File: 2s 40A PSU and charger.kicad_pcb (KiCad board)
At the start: 4 copper layers, 45 x 20 mm, 112 parts, among them J1 Keystone 3579, J10 G-Switch-GT-USB-7025, J11 1.27mm 4 pin socket, J12 USB, J2 JST XH-S Balance Plug, J3 Keystone 3579, J4 Keystone 3569, J5 Keystone 3569, J6 Keystone 3579, J7 Keystone 3579, J8 Keystone 3569, J9 Keystone 3569, Q1 PJA3430, or HL 2320A, Q2 PJA3430, or HL 2320A, Q3 Vishay sir404dp, or SiR500DP, Q4 PJA3430, or HL 2320A, Q5 PJA3430, or HL 2320A, Q6 Vishay sir404dp, or SiR500DP, U1 BQ76905RGRR, U2 AP63203WU, U3 BQ24780SRUYR, U5 THVD1420DRLR, U6 CH32X035G8U6, U7 TPS7A2633DRV

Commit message: Started layout of new components
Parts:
- added R13: 10k, Resistor_SMD:R_0402_1005Metric, B.Cu at (116.9, 130.9)
- added R32: 10k, Resistor_SMD:R_0402_1005Metric, B.Cu at (111.6, 128.1)
- added SW1: Mitsumi R-667996, Misumi switches:R-667995_MIT, B.Cu at (119.6, 130.8)
- J1, J3, J6, J7: value Keystone 3579 -> Keystone 6100; footprint custom_Connector:Keystone_3579 -> custom_Connector:Keystone_6100
- J4, J5, J8, J9: value Keystone 3569 -> Keystone 6102; footprint custom_Connector:Keystone_3569_half -> custom_Connector:Keystone_6102
- L3: value 2.2uH, WIP322512A-2R2MLDG -> 2.7uH
- U6: footprint Package_DFN_QFN:QFN-28-1EP_4x4mm_P0.4mm_EP2.8x2.8mm -> qfn_custom:QFN-28-1EP_4x4mm_P0.4mm_EP2.8x2.8mm
- moved R31 0.45 mm to (115.1, 130.9)
- moved R30 0.43 mm to (113.3, 131.0)
- moved D2 0.39 mm to (111.2, 129.8)
- moved U2 0.18 mm to (134.1, 121.0)
- moved C40 0.17 mm to (133.5, 118.5)
- moved L3 0.15 mm to (130.7, 120.8)
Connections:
- net /Battery Balancer/+BAT renamed +BATT
- net /Battery Balancer/-BAT renamed -BATT
- net /Battery Balancer/Balancer Alert renamed /Balancer_Alert
- net /Battery Balancer/Bat Cell 1 renamed /Bat Cell 1
- net /Battery Charger/Always On PWR renamed Always On PWR
- net /Battery Charger/Charger IADP renamed /Charger_IADP
- net /Battery Charger/Charger IDCHG renamed /Charger_IDCHG
- net /Battery Charger/Charger PROCHOT renamed /Charger_PROCHOT
- net /Battery Charger/IN renamed USBPWR
- net /Battery Charger/MCU3.3v renamed Always On 3v3
- net /Battery Charger/PWRON renamed /PWRON
- net /Connectors/3.3v renamed Main 3v3
- net /Connectors/CC1 renamed /CC1
- net /Connectors/CC2 renamed /CC2
- net /Connectors/D+ renamed /D+
- net /Connectors/D- renamed /D-
- net /Connectors/RS485+ renamed /RS485+
- net /Connectors/RS485- renamed /RS485-
- C12 pad 2: /Battery Charger/MOTORPWR -> MOTORPWR
- C14 pad 2: /Battery Charger/MOTORPWR -> MOTORPWR
- C28 pad 1: /Battery Charger/MOTORPWR -> MOTORPWR
- J1 pad 1: /Battery Charger/MOTORPWR -> MOTORPWR
- J3 pad 1: /Battery Charger/MOTORPWR -> MOTORPWR
- J4 pad 1: /Battery Charger/MOTORPWR -> MOTORPWR
- J5 pad 1: /Battery Charger/MOTORPWR -> MOTORPWR
- NT3 pad 2: /Battery Charger/MOTORPWR -> MOTORPWR
- NT4 pad 2: /Battery Charger/MOTORPWR -> MOTORPWR
- Q3 pad 5: /Battery Charger/MOTORPWR -> MOTORPWR
- R1 pad 1: /Battery Charger/MOTORPWR -> MOTORPWR
- U2 pad 2: /Battery Charger/MOTORPWR -> /3v3_Main_EN
- U2 pad 3: /Battery Charger/MOTORPWR -> MOTORPWR
- U6 pad 23: unconnected-(U6-PB12-Pad23) -> /3v3_Main_EN
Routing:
- net /Battery Charger/MOTORPWR: track 10.7 -> 0.00 mm, vias 1 -> 0
- net MOTORPWR: track 0.00 -> 9.46 mm, vias 0 -> 1
- net Always On 3v3: track 43.8 -> 52.3 mm
- net /3v3_Main_EN: track 0.00 -> 6.62 mm, vias 0 -> 1
- net GND: track 66.4 -> 70.2 mm, vias 47 -> 46
- net Main 3v3: track 32.4 -> 33.9 mm
- net +BATT: track 63.7 -> 62.4 mm
- net Net-(R13-Pad1): track 0.00 -> 1.26 mm
- net /D+: track 23.4 -> 24.1 mm, vias 1 -> 2
- net Net-(U3-CMPIN): track 4.11 -> 3.40 mm
- added copper zone on F.Cu, net MOTORPWR
- removed copper zone on F.Cu, net /Battery Charger/MOTORPWR

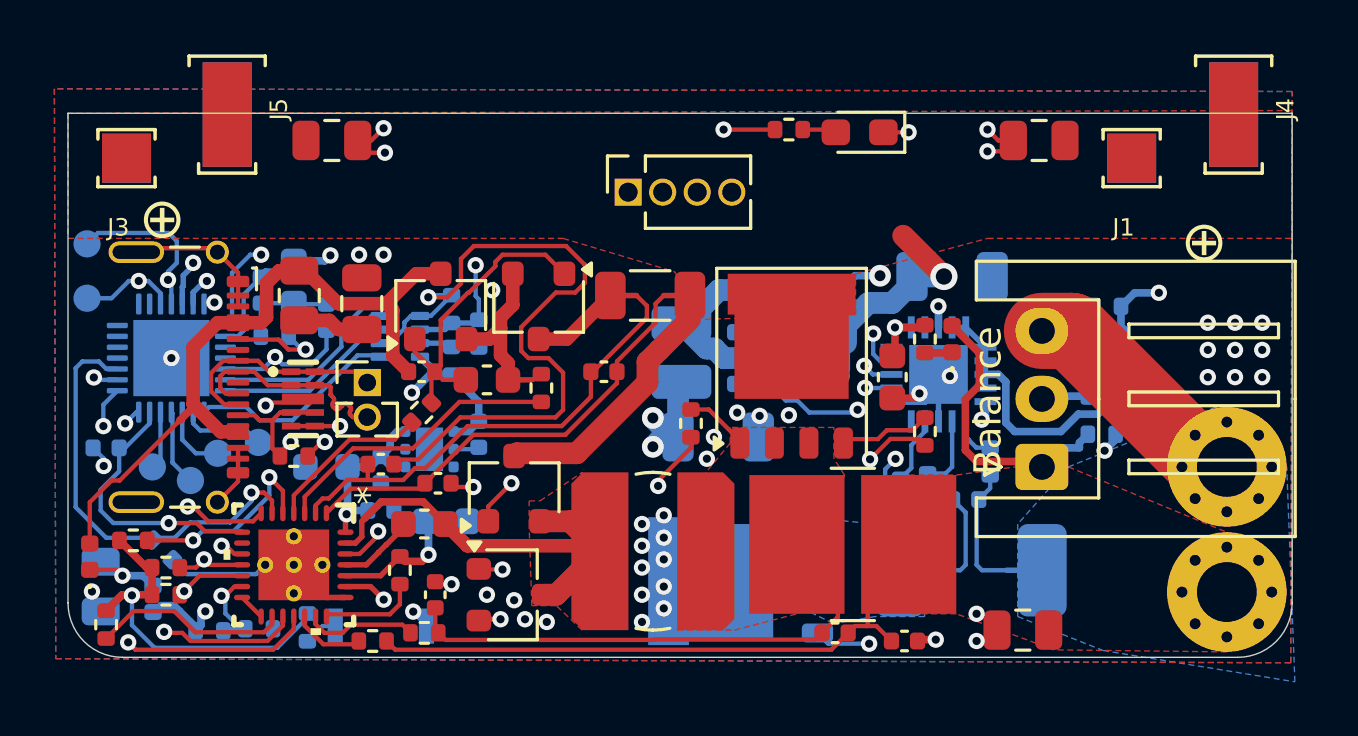
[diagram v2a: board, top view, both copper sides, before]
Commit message: Finished reroute and placement
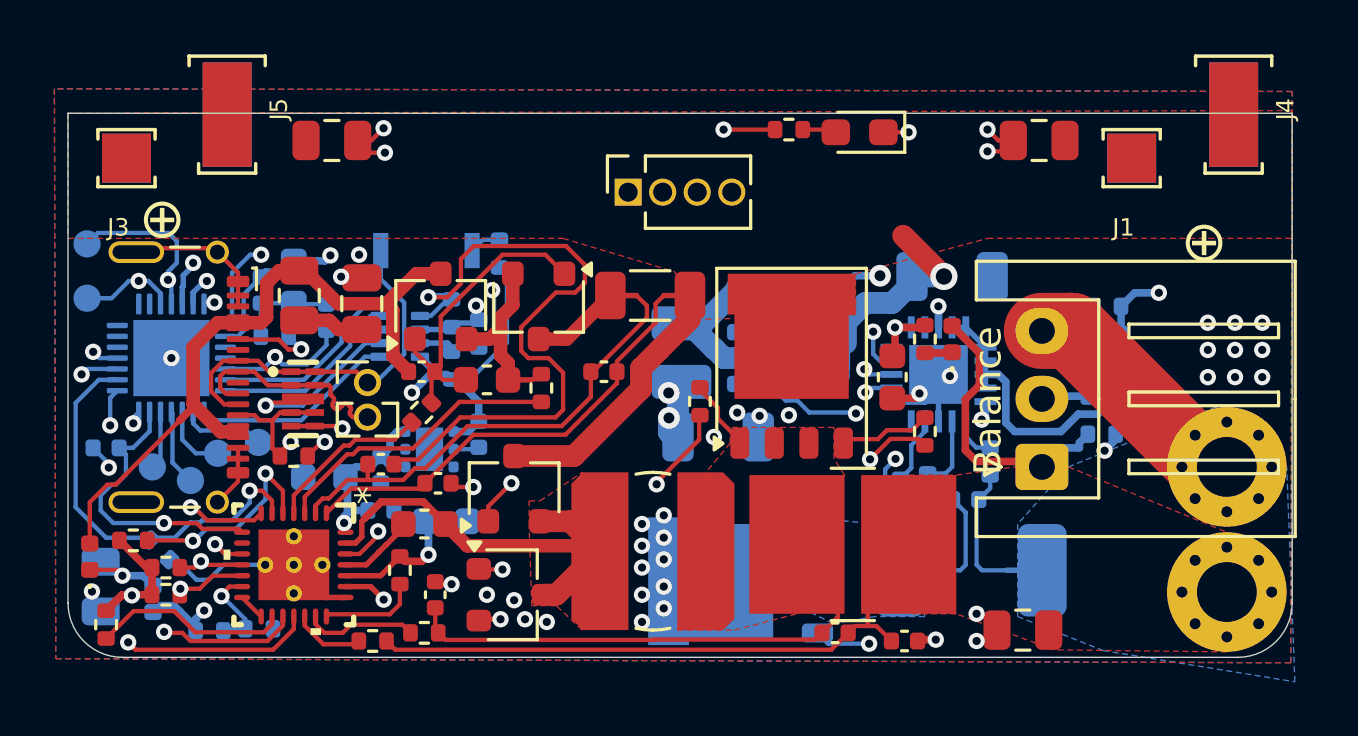
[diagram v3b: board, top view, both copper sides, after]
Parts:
- moved R13 15.4 mm to (124.0, 117.2), turned to -90 degrees
- moved SW1 13.9 mm to (121.3, 117.0), turned to 0 degrees
- moved R12 0.87 mm to (131.3, 122.6)
- moved C31 0.38 mm to (117.5, 125.4)
- moved R28 0.18 mm to (122.2, 121.3)
- moved R26 0.15 mm to (122.2, 119.3)
- moved R32 0.10 mm to (111.5, 128.1)
- moved C40 0.07 mm to (133.5, 118.6)
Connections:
- U6 pad 16: /MCU/LED -> /PWRON
- U6 pad 17: /PWRON -> /3v3_Main_EN
- U6 pad 18: unconnected-(U6-PB7-Pad18) -> /MCU/LED
- U6 pad 23: /3v3_Main_EN -> unconnected-(U6-PB12-Pad23)
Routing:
- net /3v3_Main_EN: track 6.62 -> 46.4 mm, vias 1 -> 2
- net Main 3v3: track 33.9 -> 28.2 mm
- net GND: track 70.2 -> 64.7 mm, vias 46 -> 45
- net /D+: track 24.1 -> 29.4 mm, vias 2 -> 1
- net /Balancer_Alert: track 37.8 -> 34.8 mm
- net /RS485-: track 17.4 -> 14.4 mm
- net Always On 3v3: track 52.3 -> 49.9 mm
- net /PWRON: track 16.0 -> 15.0 mm
- net /MCU/LED: track 32.7 -> 31.8 mm
- net Net-(U3-BATSRC): track 28.2 -> 29.0 mm
- net /SDA: track 52.3 -> 52.9 mm
- net /Charger_IADP: track 15.3 -> 14.8 mm

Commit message: Fixed silkscreen
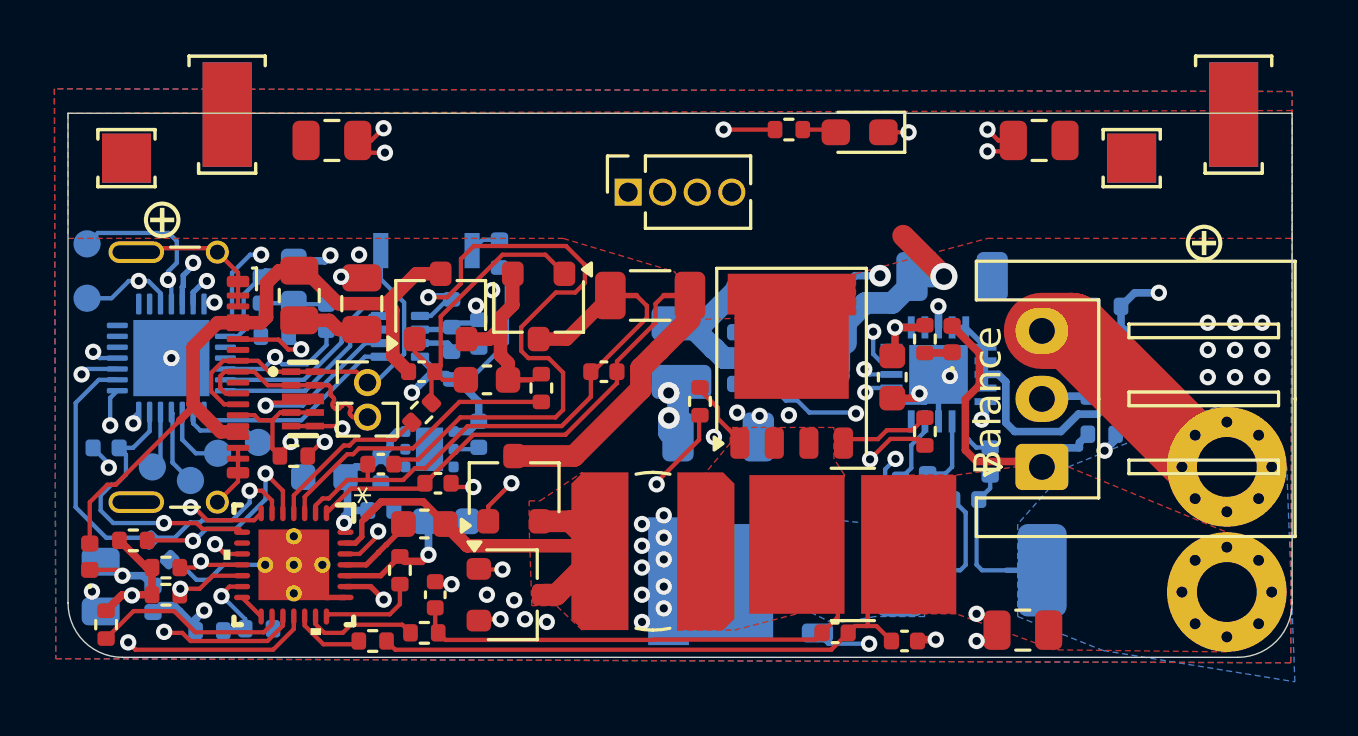
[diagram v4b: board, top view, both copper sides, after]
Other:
- board text added: "2s 40A PSU${REVISION}"
- board text added: "SDO"
- board text added: "©2025 Asher Edwards"
- board text removed: "2s 40A PSU"
- board text removed: "©2024 Asher Edwards"

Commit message: Arranged power connectors
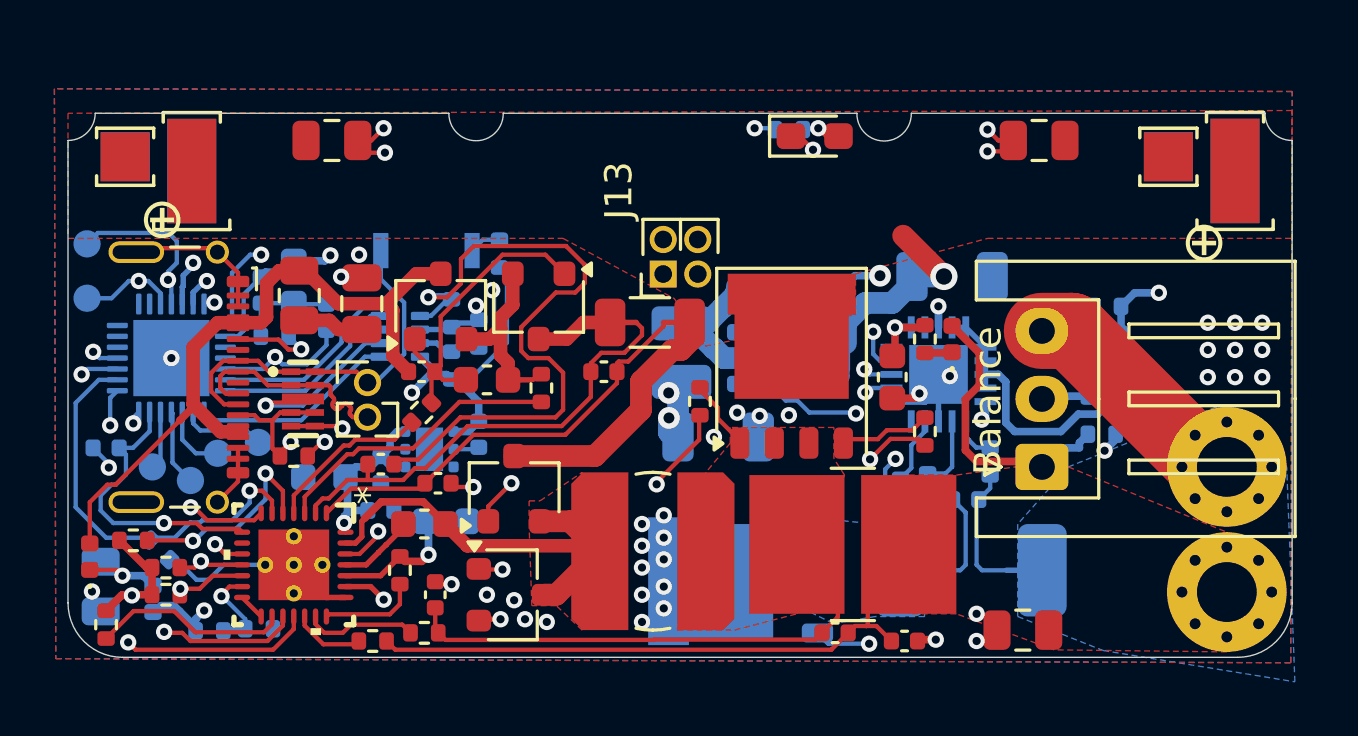
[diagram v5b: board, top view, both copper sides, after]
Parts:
- removed J11: 1.27mm 4 pin socket, Connector_PinSocket_1.27mm:PinSocket_1x04_P1.27mm_Vertical
- added J13: Precidip 853-87-004-20-001101, custom_Connector:Precidip 853-87-004-20-001101, F.Cu at (130.0, 117.9)
- R25: moved to B.Cu
- moved J5 2.45 mm to (112.7, 114.1), turned to 180 degrees
- moved J9 2.45 mm to (112.7, 114.1), turned to 0 degrees
- moved J4 2.07 mm to (151.0, 114.1), turned to 180 degrees
- moved J8 2.07 mm to (151.0, 114.1), turned to 0 degrees
- moved D4 1.66 mm to (135.6, 112.8), turned to 0 degrees
- moved J1 1.35 mm to (148.6, 113.6)
- moved J6 1.35 mm to (148.6, 113.6)
- moved NT4 1.30 mm to (129.8, 121.3)
- moved NT2 0.99 mm to (128.8, 119.7)
- moved NT3 0.99 mm to (130.2, 119.7)
- moved R1 0.99 mm to (129.5, 119.7)
- moved J3 0.07 mm to (110.2, 113.6)
- moved J7 0.07 mm to (110.2, 113.6)
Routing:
- net /RS485+: track 17.5 -> 13.0 mm
- net MOTORPWR: track 9.53 -> 11.1 mm
- net /RS485-: track 14.4 -> 13.0 mm
- net /D+: track 29.4 -> 28.2 mm
- net Net-(Q4-D): track 7.39 -> 6.44 mm
- net Net-(U3-ACN): track 16.6 -> 15.9 mm
- net Net-(U3-ACP): track 17.4 -> 16.7 mm
- net Main 3v3: track 28.2 -> 27.7 mm
- net Net-(D4-A): track 1.26 -> 1.46 mm, vias 0 -> 1
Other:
- outline, holes or cut-outs redrawn
